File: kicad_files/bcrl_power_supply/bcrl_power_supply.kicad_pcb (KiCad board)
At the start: 2 copper layers, 9 parts, among them J1 OSTVN02A150, J2 OSTVN02A150, J3 OSTVN02A150, J4 OSTVN02A150, J5 OSTVN02A150, J6 OSTVN02A150, J7 OSTVN02A150

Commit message: ...
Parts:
- added CJ2: Conn_01x10, Connector_PinSocket_2.54mm:PinSocket_1x10_P2.54mm_Vertical, F.Cu at (129.5, 66.0)
- added P1: Conn_01x10, Connector_PinSocket_1.27mm:PinSocket_1x10_P1.27mm_Vertical, F.Cu at (138.7, 65.4)
- added PJ1: Conn_01x10, Connector_PinSocket_2.54mm:PinSocket_1x10_P2.54mm_Vertical, F.Cu at (134.1, 66.0)
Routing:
- net (no net): vias 1 -> 0

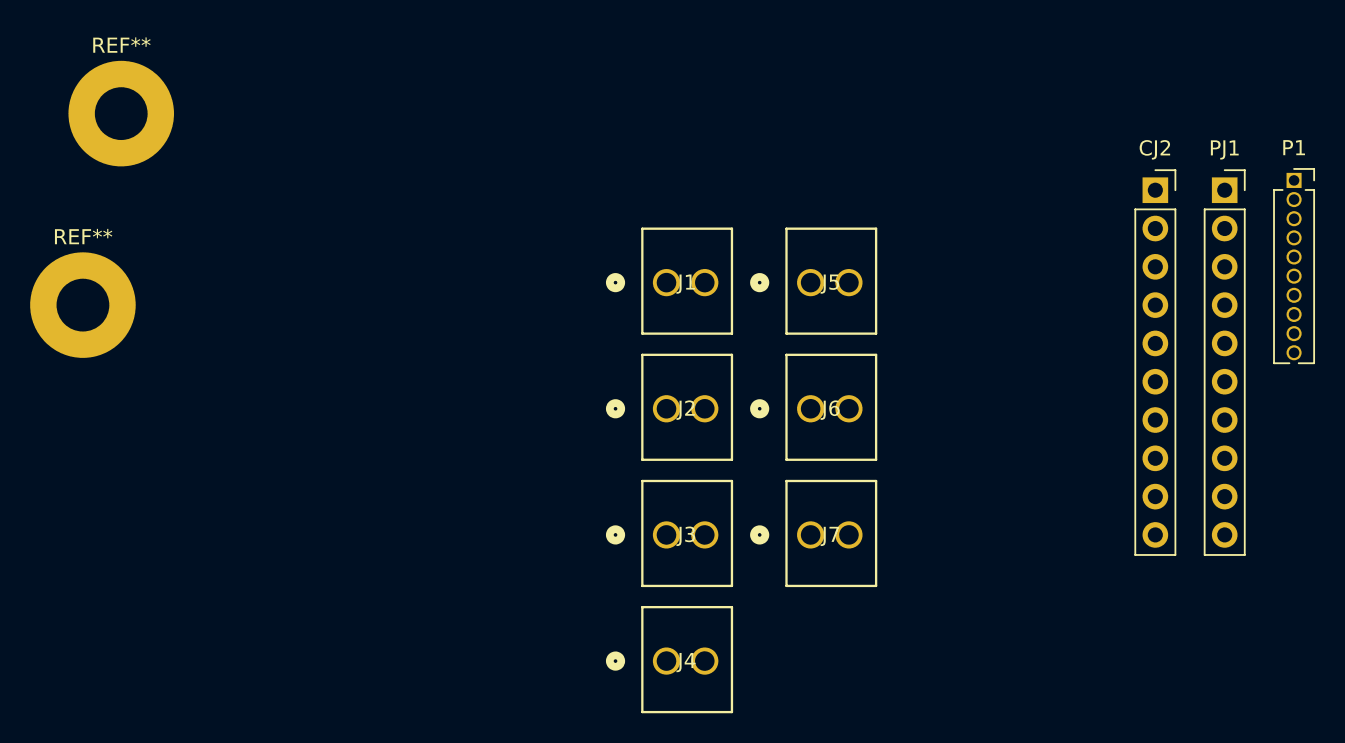
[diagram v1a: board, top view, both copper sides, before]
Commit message: added components
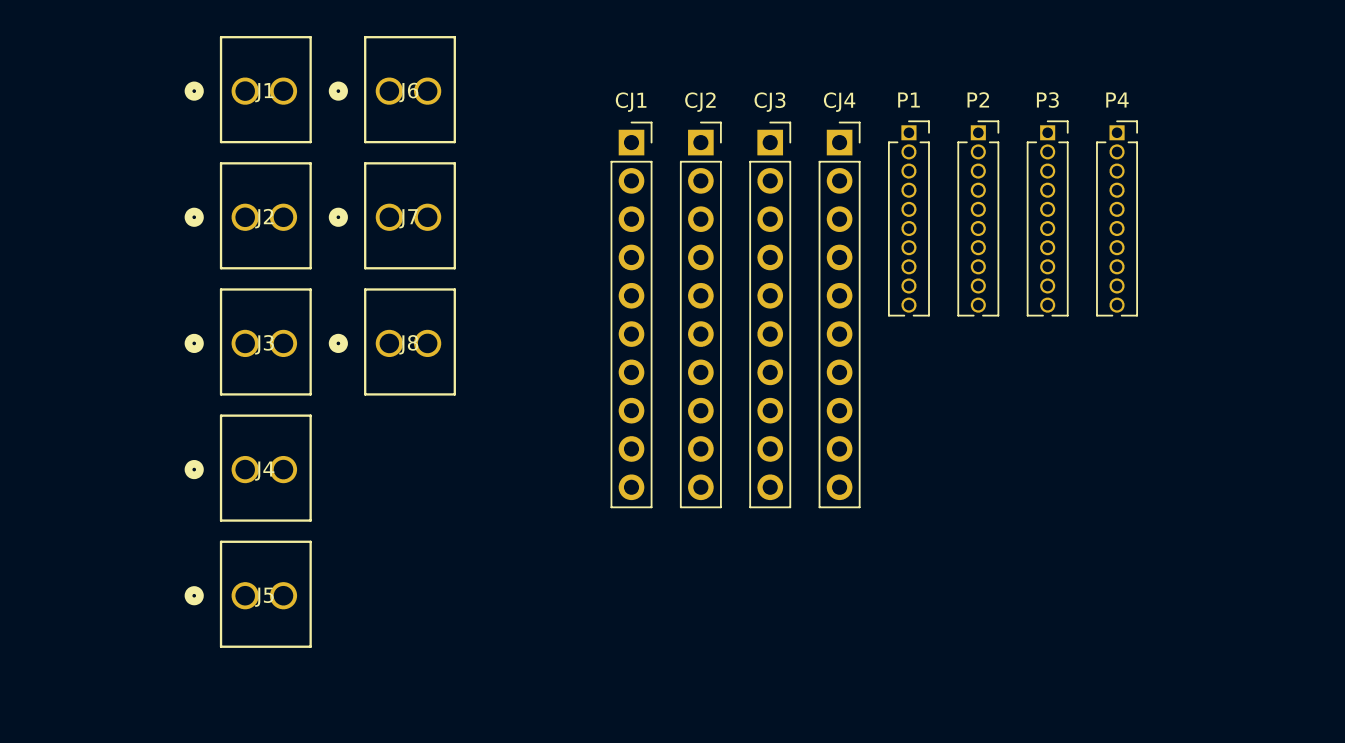
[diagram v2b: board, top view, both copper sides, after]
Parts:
- removed PJ1: Conn_01x10, Connector_PinSocket_2.54mm:PinSocket_1x10_P2.54mm_Vertical
- removed REF** (x2): MountingHole_3.5mm_Pad, MountingHole:MountingHole_3.5mm_Pad
- added CJ1: Conn_01x10, Connector_PinSocket_2.54mm:PinSocket_1x10_P2.54mm_Vertical, F.Cu at (94.8, 62.9)
- added CJ3: Conn_01x10, Connector_PinSocket_2.54mm:PinSocket_1x10_P2.54mm_Vertical, F.Cu at (104.0, 62.9)
- added CJ4: Conn_01x10, Connector_PinSocket_2.54mm:PinSocket_1x10_P2.54mm_Vertical, F.Cu at (108.6, 62.9)
- added J8: OSTVN02A150, BCRL_power_supply:CONN_OSTVN02A150_OST, F.Cu at (78.7, 76.2)
- added P2: Conn_01x10, Connector_PinSocket_1.27mm:PinSocket_1x10_P1.27mm_Vertical, F.Cu at (117.8, 62.2)
- added P3: Conn_01x10, Connector_PinSocket_1.27mm:PinSocket_1x10_P1.27mm_Vertical, F.Cu at (122.4, 62.2)
- added P4: Conn_01x10, Connector_PinSocket_1.27mm:PinSocket_1x10_P1.27mm_Vertical, F.Cu at (127.0, 62.2)
- J1, J2, J3, J4, J5, J6, J7: footprint screw_terminal:CONN_OSTVN02A150_OST -> BCRL_power_supply:CONN_OSTVN02A150_OST
- moved J5 42.9 mm to (69.2, 92.9)
- moved J6 35.0 mm to (78.7, 59.5)
- moved J7 35.0 mm to (78.7, 67.8)
- moved J1 30.7 mm to (69.2, 59.5)
- moved J2 30.7 mm to (69.2, 67.8)
- moved J3 30.7 mm to (69.2, 76.2)
- moved J4 30.7 mm to (69.2, 84.6)
- moved CJ2 30.3 mm to (99.4, 62.9)
- moved P1 25.7 mm to (113.2, 62.2)
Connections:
- J1 pad 1: unconnected-(J1-Pad1) -> 48V
- J1 pad 2: unconnected-(J1-Pad2) -> 48V
- J2 pad 1: unconnected-(J2-Pad1) -> 48V
- J2 pad 2: unconnected-(J2-Pad2) -> 48V
- J3 pad 1: unconnected-(J3-Pad1) -> GND
- J3 pad 2: unconnected-(J3-Pad2) -> GND
- J4 pad 1: unconnected-(J4-Pad1) -> GND
- J4 pad 2: unconnected-(J4-Pad2) -> GND

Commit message: fixed path
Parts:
- added PS1: PYBE20-Q48-S9, BCRL_power_supply:CONV_PYBE20-Q48-S9, F.Cu at (193.0, -41.5)
- added PS2: PYBE20-Q48-S9, BCRL_power_supply:CONV_PYBE20-Q48-S9, F.Cu at (193.0, -14.5)
- added PS3: PYBE20-Q48-S9, BCRL_power_supply:CONV_PYBE20-Q48-S9, F.Cu at (193.0, 12.4)
- added PS4: PYBE20-Q48-S9, BCRL_power_supply:CONV_PYBE20-Q48-S9, F.Cu at (193.0, 39.4)
- added PS5: PYBE20-Q48-S5, BCRL_power_supply:CONV_PYBE20-Q48-S5, F.Cu at (193.0, 66.3)
- added PS6: PYBE20-Q48-S5, BCRL_power_supply:CONV_PYBE20-Q48-S5, F.Cu at (193.0, 93.3)
- added PS7: PYBE20-Q48-S5, BCRL_power_supply:CONV_PYBE20-Q48-S5, F.Cu at (193.0, 120.2)
- added PS8: PYBE20-Q48-S5, BCRL_power_supply:CONV_PYBE20-Q48-S5, F.Cu at (193.0, 147.2)
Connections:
- J1 pad 1: 48V -> unconnected-(J1-Pad1)
- J1 pad 2: 48V -> unconnected-(J1-Pad2)
- J2 pad 1: 48V -> unconnected-(J2-Pad1)
- J2 pad 2: 48V -> unconnected-(J2-Pad2)
- J3 pad 1: GND -> unconnected-(J3-Pad1)
- J3 pad 2: GND -> unconnected-(J3-Pad2)
- J4 pad 1: GND -> unconnected-(J4-Pad1)
- J4 pad 2: GND -> unconnected-(J4-Pad2)

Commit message: TxMUX done
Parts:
- removed CJ1, CJ2, CJ3, CJ4: Conn_01x10, Connector_PinSocket_2.54mm:PinSocket_1x10_P2.54mm_Vertical
- added J11: 5034801600, BCRL_power_supply:MOLEX_5034801600, F.Cu at (235.0, 155.8)
- added J9: 5034801600, BCRL_power_supply:MOLEX_5034801600, F.Cu at (235.0, 150.0)
- added PS11: PQC50-48-S5-O, BCRL_power_supply:CONV_PQC50-48-S5-O, F.Cu at (220.4, 134.6)
- added PS9: EHHD010A0B41-HZ, BCRL_power_supply:CONV_EHHD010A0B41-HZ, F.Cu at (233.4, 67.5)
- added U1: PDQ10-Q48-S3-D, BCRL_power_supply:CONV_PDQ10-Q48-S3-D, F.Cu at (215.9, 161.7)
- P1, P2, P3, P4: value Conn_01x10 -> 5104338-1; footprint Connector_PinSocket_1.27mm:PinSocket_1x10_P1.27mm_Vertical -> BCRL_power_supply:TE_5104338-1
- moved J1 162.1 mm to (229.4, 83.9)
- moved J2 162.1 mm to (229.4, 92.3)
- moved J3 162.1 mm to (229.4, 100.7)
- moved J4 162.1 mm to (229.4, 109.0)
- moved J5 162.1 mm to (229.4, 117.4)
- moved J6 162.1 mm to (238.9, 83.9)
- moved J7 162.1 mm to (238.9, 92.3)
- moved J8 162.1 mm to (238.9, 100.7)
- moved PS5 111.5 mm to (176.3, 176.6)
- moved PS7 111.5 mm to (176.3, 230.5)
- moved PS8 111.5 mm to (176.3, 257.4)
- moved PS2 111.5 mm to (176.3, 95.7)
- moved PS3 111.5 mm to (176.3, 122.7)
- moved PS6 111.5 mm to (176.3, 203.5)
- moved PS1 111.5 mm to (176.3, 68.8)
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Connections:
- J1 pad 1: unconnected-(J1-Pad1) -> +5V
- J1 pad 2: unconnected-(J1-Pad2) -> GND
- J2 pad 1: unconnected-(J2-Pad1) -> +5V
- J2 pad 2: unconnected-(J2-Pad2) -> GND
- J3 pad 1: unconnected-(J3-Pad1) -> +5V
- J3 pad 2: unconnected-(J3-Pad2) -> GND
- J4 pad 1: unconnected-(J4-Pad1) -> +5V
- J4 pad 2: unconnected-(J4-Pad2) -> GND
- J5 pad 1: unconnected-(J5-Pad1) -> +8V
- J5 pad 2: unconnected-(J5-Pad2) -> GND
- J6 pad 1: unconnected-(J6-Pad1) -> +8V
- J6 pad 2: unconnected-(J6-Pad2) -> GND
- J7 pad 1: unconnected-(J7-Pad1) -> +8V
- J7 pad 2: unconnected-(J7-Pad2) -> GND
- J8 pad 1: unconnected-(J8-Pad1) -> +8V
- J8 pad 2: unconnected-(J8-Pad2) -> GND
- P1 pad 1: unconnected-(P1-Pin_1-Pad1) -> /TxRFswMUXv1 board/P1.1_VCTL2_SW1
- P1 pad 2: unconnected-(P1-Pin_2-Pad2) -> /TxRFswMUXv1 board/P1.2_VCTL2_SW2
- P1 pad 3: unconnected-(P1-Pin_3-Pad3) -> /TxRFswMUXv1 board/P1.3_VCTL1
- P1 pad 4: unconnected-(P1-Pin_4-Pad4) -> GND
- P1 pad 5: unconnected-(P1-Pin_5-Pad5) -> +3.3V
- P1 pad 6: unconnected-(P1-Pin_6-Pad6) -> GND
- P2 pad 1: unconnected-(P2-Pin_1-Pad1) -> /TxRFswMUXv1 board/P2.1_VCTL2_SW1
- P2 pad 2: unconnected-(P2-Pin_2-Pad2) -> /TxRFswMUXv1 board/P2.1_VCTL2_SW1
- P2 pad 3: unconnected-(P2-Pin_3-Pad3) -> /TxRFswMUXv1 board/P2.3_VCTL1
- P2 pad 4: unconnected-(P2-Pin_4-Pad4) -> GND
- P2 pad 5: unconnected-(P2-Pin_5-Pad5) -> +3.3V
- P2 pad 6: unconnected-(P2-Pin_6-Pad6) -> GND
- P3 pad 1: unconnected-(P3-Pin_1-Pad1) -> /TxRFswMUXv1 board/P3.1_VCTL2_SW1
- P3 pad 2: unconnected-(P3-Pin_2-Pad2) -> /TxRFswMUXv1 board/P3.1_VCTL2_SW1
- P3 pad 3: unconnected-(P3-Pin_3-Pad3) -> /TxRFswMUXv1 board/P3.3_VCTL1
- P3 pad 4: unconnected-(P3-Pin_4-Pad4) -> GND
- P3 pad 5: unconnected-(P3-Pin_5-Pad5) -> +3.3V
- P3 pad 6: unconnected-(P3-Pin_6-Pad6) -> GND
- P4 pad 1: unconnected-(P4-Pin_1-Pad1) -> /TxRFswMUXv1 board/P4.1_VCTL2_SW1
- P4 pad 2: unconnected-(P4-Pin_2-Pad2) -> /TxRFswMUXv1 board/P4.1_VCTL2_SW1
- P4 pad 3: unconnected-(P4-Pin_3-Pad3) -> /TxRFswMUXv1 board/P4.3_VCTL1
- P4 pad 4: unconnected-(P4-Pin_4-Pad4) -> GND
- P4 pad 5: unconnected-(P4-Pin_5-Pad5) -> +3.3V
- P4 pad 6: unconnected-(P4-Pin_6-Pad6) -> GND
- PS5 pad 5: unconnected-(PS5-0V-Pad5) -> GND
- PS6 pad 5: unconnected-(PS6-0V-Pad5) -> GND
- PS7 pad 5: unconnected-(PS7-0V-Pad5) -> GND
- PS8 pad 5: unconnected-(PS8-0V-Pad5) -> GND

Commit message: added EMC
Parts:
- added C1: 330uf/100v, Capacitor_SMD:C_0603_1608Metric, F.Cu at (-16.9, 121.0)
- added C10: 1nf/2kv, Capacitor_SMD:C_0603_1608Metric, F.Cu at (-16.9, 172.5)
- added C11: 1nf/2kv, Capacitor_SMD:C_0603_1608Metric, F.Cu at (-16.9, 175.0)
- added C12: 470uf, Capacitor_SMD:C_0603_1608Metric, F.Cu at (-16.9, 177.5)
- added C13: 4.7uf/100v, Capacitor_SMD:C_0603_1608Metric, F.Cu at (140.2, 94.0)
- added C14: 4.7uf/100uf, Capacitor_SMD:C_0603_1608Metric, F.Cu at (140.2, 96.5)
- added C15: 330uf/100v, Capacitor_SMD:C_0603_1608Metric, F.Cu at (-16.9, 77.0)
- added C16: 100uf, Capacitor_SMD:C_0603_1608Metric, F.Cu at (-16.9, 79.5)
- added C17: 100uf, Capacitor_SMD:C_0603_1608Metric, F.Cu at (-16.9, 82.0)
- added C18: 1nf/2kv, Capacitor_SMD:C_0603_1608Metric, F.Cu at (-16.9, 84.5)
- added C19: 1nf/2kv, Capacitor_SMD:C_0603_1608Metric, F.Cu at (-16.9, 87.0)
- added C2: 100uf, Capacitor_SMD:C_0603_1608Metric, F.Cu at (-16.9, 123.5)
- added C20: 470uf, Capacitor_SMD:C_0603_1608Metric, F.Cu at (-16.9, 89.5)
- added C21: 330uf/100v, Capacitor_SMD:C_0603_1608Metric, F.Cu at (38.8, 77.0)
- added C22: 100uf, Capacitor_SMD:C_0603_1608Metric, F.Cu at (38.8, 79.5)
- added C23: 100uf, Capacitor_SMD:C_0603_1608Metric, F.Cu at (38.8, 82.0)
- added C24: 1nf/2kv, Capacitor_SMD:C_0603_1608Metric, F.Cu at (38.8, 84.5)
- added C25: 1nf/2kv, Capacitor_SMD:C_0603_1608Metric, F.Cu at (38.8, 87.0)
- added C26: 470uf, Capacitor_SMD:C_0603_1608Metric, F.Cu at (38.8, 89.5)
- added C27: 680uf/100v, Capacitor_SMD:C_0603_1608Metric, F.Cu at (76.0, 118.4)
- added C28: 4.7uf/100v, Capacitor_SMD:C_0603_1608Metric, F.Cu at (76.0, 120.9)
- added C29: 4.7uf/100v, Capacitor_SMD:C_0603_1608Metric, F.Cu at (76.0, 123.5)
- added C3: 100uf, Capacitor_SMD:C_0603_1608Metric, F.Cu at (-16.9, 126.0)
- added C30: 4.7uf/100v, Capacitor_SMD:C_0603_1608Metric, F.Cu at (76.0, 126.0)
- added C31: 4.7uf/100v, Capacitor_SMD:C_0603_1608Metric, F.Cu at (76.0, 128.5)
- added C32: 2.2nf/400vac, Capacitor_SMD:C_0603_1608Metric, F.Cu at (76.0, 131.0)
- added C33: 2.2nf/400vac, Capacitor_SMD:C_0603_1608Metric, F.Cu at (80.0, 118.4)
- added C34: 330uf/63v, Capacitor_SMD:C_0603_1608Metric, F.Cu at (80.0, 120.9)
- added C35: 680uf/100v, Capacitor_SMD:C_0603_1608Metric, F.Cu at (38.8, 159.9)
- added C36: 4.7uf/100v, Capacitor_SMD:C_0603_1608Metric, F.Cu at (38.8, 162.4)
- added C37: 4.7uf/100v, Capacitor_SMD:C_0603_1608Metric, F.Cu at (38.8, 164.9)
- added C38: 4.7uf/100v, Capacitor_SMD:C_0603_1608Metric, F.Cu at (38.8, 167.4)
- added C39: 4.7uf/100v, Capacitor_SMD:C_0603_1608Metric, F.Cu at (38.8, 169.9)
- added C4: 1nf/2kv, Capacitor_SMD:C_0603_1608Metric, F.Cu at (-16.9, 128.5)
- added C40: 2.2nf/400vac, Capacitor_SMD:C_0603_1608Metric, F.Cu at (38.8, 172.4)
- added C41: 2.2nf/400vac, Capacitor_SMD:C_0603_1608Metric, F.Cu at (42.8, 159.9)
- added C42: 330uf/63v, Capacitor_SMD:C_0603_1608Metric, F.Cu at (42.8, 162.4)
- added C43: 680uf/100v, Capacitor_SMD:C_0603_1608Metric, F.Cu at (94.5, 74.4)
- added C44: 4.7uf/100v, Capacitor_SMD:C_0603_1608Metric, F.Cu at (94.5, 76.9)
- added C45: 4.7uf/100v, Capacitor_SMD:C_0603_1608Metric, F.Cu at (94.5, 79.4)
- added C46: 4.7uf/100v, Capacitor_SMD:C_0603_1608Metric, F.Cu at (94.5, 82.0)
- added C47: 4.7uf/100v, Capacitor_SMD:C_0603_1608Metric, F.Cu at (94.5, 84.5)
- added C48: 2.2nf/400vac, Capacitor_SMD:C_0603_1608Metric, F.Cu at (94.5, 87.0)
- added C49: 2.2nf/400vac, Capacitor_SMD:C_0603_1608Metric, F.Cu at (98.6, 74.4)
- added C5: 1nf/2kv, Capacitor_SMD:C_0603_1608Metric, F.Cu at (-16.9, 131.0)
- added C50: 330uf/63v, Capacitor_SMD:C_0603_1608Metric, F.Cu at (98.6, 76.9)
- added C51: 680uf/100v, Capacitor_SMD:C_0603_1608Metric, F.Cu at (38.8, 118.4)
- added C52: 4.7uf/100v, Capacitor_SMD:C_0603_1608Metric, F.Cu at (38.8, 120.9)
- added C53: 4.7uf/100v, Capacitor_SMD:C_0603_1608Metric, F.Cu at (38.8, 123.5)
- added C54: 4.7uf/100v, Capacitor_SMD:C_0603_1608Metric, F.Cu at (38.8, 126.0)
- added C55: 4.7uf/100v, Capacitor_SMD:C_0603_1608Metric, F.Cu at (38.8, 128.5)
- added C56: 2.2nf/400vac, Capacitor_SMD:C_0603_1608Metric, F.Cu at (38.8, 131.0)
- added C57: 2.2nf/400vac, Capacitor_SMD:C_0603_1608Metric, F.Cu at (42.8, 118.4)
- added C58: 330uf/63v, Capacitor_SMD:C_0603_1608Metric, F.Cu at (42.8, 120.9)
- added C6: 470uf, Capacitor_SMD:C_0603_1608Metric, F.Cu at (-16.9, 133.5)
- added C7: 330uf/100v, Capacitor_SMD:C_0603_1608Metric, F.Cu at (-16.9, 165.0)
- added C8: 100uf, Capacitor_SMD:C_0603_1608Metric, F.Cu at (-16.9, 167.5)
- added C9: 100uf, Capacitor_SMD:C_0603_1608Metric, F.Cu at (-16.9, 170.0)
- added PS1: PYBE20-Q48-S5, BCRL_power_supply:CONV_PYBE20-Q48-S5, F.Cu at (8.63, 106.2)
- added PS2: PYBE20-Q48-S5, BCRL_power_supply:CONV_PYBE20-Q48-S5, F.Cu at (8.63, 150.2)
- added PS3: PYBE20-Q48-S5, BCRL_power_supply:CONV_PYBE20-Q48-S5, F.Cu at (8.63, 62.2)
- added PS4: EHHD010A0B41-HZ, BCRL_power_supply:CONV_EHHD010A0B41-HZ, F.Cu at (105.0, 146.4)
- added PS5: PYBE20-Q48-S5, BCRL_power_supply:CONV_PYBE20-Q48-S5, F.Cu at (64.4, 62.2)
- added PS6: PQC50-48-S5-O, BCRL_power_supply:CONV_PQC50-48-S5-O, F.Cu at (92.0, 105.0)
- added PS7: PQC50-48-S5-O, BCRL_power_supply:CONV_PQC50-48-S5-O, F.Cu at (54.8, 146.4)
- added PS8: PQC50-48-S5-O, BCRL_power_supply:CONV_PQC50-48-S5-O, F.Cu at (110.5, 61.0)
- added PS9: PQC50-48-S5-O, BCRL_power_supply:CONV_PQC50-48-S5-O, F.Cu at (54.8, 105.0)
- added R1: R, Resistor_SMD:R_0603_1608Metric, F.Cu at (80.0, 123.5)
- added R10: R, Resistor_SMD:R_0603_1608Metric, F.Cu at (42.8, 123.5)
- added R11: R, Resistor_SMD:R_0603_1608Metric, F.Cu at (42.8, 126.0)
- added R12: R, Resistor_SMD:R_0603_1608Metric, F.Cu at (42.8, 128.5)
- added R2: R, Resistor_SMD:R_0603_1608Metric, F.Cu at (80.0, 126.0)
- added R3: R, Resistor_SMD:R_0603_1608Metric, F.Cu at (80.0, 128.5)
- added R4: R, Resistor_SMD:R_0603_1608Metric, F.Cu at (42.8, 164.9)
- added R5: R, Resistor_SMD:R_0603_1608Metric, F.Cu at (42.8, 167.4)
- added R6: R, Resistor_SMD:R_0603_1608Metric, F.Cu at (42.8, 169.9)
- added R7: R, Resistor_SMD:R_0603_1608Metric, F.Cu at (98.6, 79.4)
- added R8: R, Resistor_SMD:R_0603_1608Metric, F.Cu at (98.6, 82.0)
- added R9: R, Resistor_SMD:R_0603_1608Metric, F.Cu at (98.6, 84.5)
- added U1: PDQ10-Q48-S3-D, BCRL_power_supply:CONV_PDQ10-Q48-S3-D, F.Cu at (124.7, 107.6)
- renumbered J8 to J10, J9 to J11, J11 to J12, J1 to J3, J2 to J4, J3 to J5, J4 to J6, J5 to J7, J6 to J8, J7 to J9, PS11 to PS10
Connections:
- J11 pad S1: unconnected-(J9-SHIELD-PadS1) -> GND
- J11 pad S2: unconnected-(J9-SHIELD__1-PadS2) -> GND
- J12 pad 6: unconnected-(J11-Pad6) -> /TxRFswMUXv1 board/TxPAx4_8V_CTL
- J12 pad 7: GND -> unconnected-(J12-Pad7)
- J12 pad 9: unconnected-(J11-Pad9) -> GND
- J12 pad S1: unconnected-(J11-SHIELD-PadS1) -> GND
- J12 pad S2: unconnected-(J11-SHIELD__1-PadS2) -> GND

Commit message: added more circuits
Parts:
- removed C1, C15, C21, C7: 330uf/100v, Capacitor_SMD:C_0603_1608Metric
- removed C10, C11, C18, C19, C24, C25, C4, C5: 1nf/2kv, Capacitor_SMD:C_0603_1608Metric
- removed C12, C20, C26, C6: 470uf, Capacitor_SMD:C_0603_1608Metric
- removed C13, C28, C29, C30, C31, C36, C37, C38, C39, C44, C45, C46, C47, C52, C53, C54, C55: 4.7uf/100v, Capacitor_SMD:C_0603_1608Metric
- removed C14: 4.7uf/100uf, Capacitor_SMD:C_0603_1608Metric
- removed C16, C17, C2, C22, C23, C3, C8, C9: 100uf, Capacitor_SMD:C_0603_1608Metric
- removed C27, C35, C43, C51: 680uf/100v, Capacitor_SMD:C_0603_1608Metric
- removed C32, C33, C40, C41, C48, C49, C56, C57: 2.2nf/400vac, Capacitor_SMD:C_0603_1608Metric
- removed C34, C42, C50, C58: 330uf/63v, Capacitor_SMD:C_0603_1608Metric
- removed J10, J3, J4, J5, J6, J7, J8, J9: OSTVN02A150, BCRL_power_supply:CONN_OSTVN02A150_OST
- removed J11, J12: 5034801600, BCRL_power_supply:MOLEX_5034801600
- removed P1, P2, P3, P4: 5104338-1, BCRL_power_supply:TE_5104338-1
- removed PS1, PS2, PS3, PS4: PYBE20-Q48-S9, BCRL_power_supply:CONV_PYBE20-Q48-S9
- removed PS1, PS2, PS3, PS5 (x2), PS6, PS7, PS8: PYBE20-Q48-S5, BCRL_power_supply:CONV_PYBE20-Q48-S5
- removed PS10, PS6, PS7, PS8, PS9: PQC50-48-S5-O, BCRL_power_supply:CONV_PQC50-48-S5-O
- removed PS4, PS9: EHHD010A0B41-HZ, BCRL_power_supply:CONV_EHHD010A0B41-HZ
- removed R1, R10, R11, R12, R2, R3, R4, R5, R6, R7, R8, R9: R, Resistor_SMD:R_0603_1608Metric
- removed U1 (x2): PDQ10-Q48-S3-D, BCRL_power_supply:CONV_PDQ10-Q48-S3-D
